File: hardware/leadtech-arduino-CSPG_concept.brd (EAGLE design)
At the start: 80 x 61 mm, 63 parts, among them IC1 OP-AMP, IC3 4050D, J1 CON_HEADER_1X08-PTH, J3 CON_HX42003_2, J5 CON_HEADER_1X02-PTH, J6 2510-4AGW, J9 CON_HEADER_1X02-PTH, Q1 16Mhz, U1 DS1302, U2 VREG-78M05, U3 PL2303HX, U4 MP1584EN_MODULE, U5 RT9163-3.3V, U6 ATMEGA1281, U7 AZ1117CH2-3.3TRG1

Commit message: 1
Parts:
- moved J3 10.7 mm to (66.2, 57.0)
- moved U2 7.24 mm to (63.5, 48.9), turned to 270 degrees
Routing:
- net +5V: track 221.0 -> 239.4 mm
- net VIN: track 44.7 -> 48.7 mm
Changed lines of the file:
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@@
 <?xml version="1.0" encoding="utf-8"?>
 <!DOCTYPE eagle SYSTEM "eagle.dtd">
-<eagle version="9.4.2">
+<eagle version="9.1.3">
 <drawing>
 <settings>
@@
 <attribute name="VALUE" x="57.912" y="21.971" size="1.27" layer="27" font="vector" ratio="10" rot="R180"/>
 </element>
-<element name="U2" library="trosh_devices.eagle.v9" package="DPAK-3" value="VREG-78M05" x="65.405" y="55.88" smashed="yes">
-<attribute name="NAME" x="65.405" y="45.72" size="1.27" layer="25" font="vector" ratio="12" rot="R180" align="center"/>
-<attribute name="VALUE" x="65.405" y="45.72" size="1.27" layer="27" font="vector" align="center"/>
+<element name="U2" library="trosh_devices.eagle.v9" package="DPAK-3" value="VREG-78M05" x="63.5" y="48.895" smashed="yes" rot="R270">
+<attribute name="NAME" x="53.34" y="48.895" size="1.27" layer="25" font="vector" ratio="12" rot="R90" align="center"/>
+<attribute name="VALUE" x="53.34" y="48.895" size="1.27" layer="27" font="vector" rot="R270" align="center"/>
 </element>
 <element name="U4" library="trosh_devices.eagle.v9" package="MP1584EN_DCDC_MODULE" value="MP1584EN_MODULE" x="67.905" y="32.385" smashed="yes" rot="R180">
@@
 <attribute name="VALUE" x="6.604" y="26.162" size="1.27" layer="27" font="vector" ratio="10" rot="R270"/>
 </element>
-<element name="J3" library="trosh_devices.eagle.v9" package="HX42003-2WAF" value="CON_HX42003_2" x="76.835" y="57.15" smashed="yes" rot="R90">
-<attribute name="NAME" x="78.105" y="60.96" size="1.27" layer="25" rot="R90"/>
-<attribute name="VALUE" x="80.645" y="60.96" size="1.27" layer="27" rot="R90"/>
+<element name="J3" library="trosh_devices.eagle.v9" package="HX42003-2WAF" value="CON_HX42003_2" x="66.167" y="57.023" smashed="yes" rot="R90">
+<attribute name="NAME" x="67.437" y="60.833" size="1.27" layer="25" rot="R90"/>
+<attribute name="VALUE" x="69.977" y="60.833" size="1.27" layer="27" rot="R90"/>
 </element>
 <element name="J6" library="trosh_devices.eagle.v9" package="KF2510-4AGW-2" value="2510-4AGW" x="11.811" y="51.435" smashed="yes" rot="R90">
@@
 <wire x1="59.385" y1="44.45" x2="63.5" y2="44.45" width="1.2192" layer="1"/>
 <wire x1="63.5" y1="44.45" x2="66.675" y2="44.45" width="1.2192" layer="1"/>
-<wire x1="67.69" y1="45.465" x2="67.69" y2="48.7" width="1.2192" layer="1"/>
+<wire x1="67.69" y1="45.465" x2="56.32" y2="46.61" width="1.2192" layer="1"/>
 <wire x1="66.675" y1="44.45" x2="67.69" y2="45.465" width="1.2192" layer="1"/>
 <wire x1="57.565" y1="59.015" x2="59.73" y2="59.015" width="0.3048" layer="1"/>
 <wire x1="60.96" y1="57.785" x2="60.96" y2="52.07" width="0.3048" layer="1"/>
 <wire x1="60.96" y1="52.07" x2="61.595" y2="51.435" width="0.3048" layer="1"/>
-<wire x1="67.69" y1="50.42" x2="67.69" y2="48.7" width="0.3048" layer="1"/>
+<wire x1="67.69" y1="50.42" x2="56.32" y2="46.61" width="0.3048" layer="1"/>
 <wire x1="59.73" y1="59.015" x2="60.96" y2="57.785" width="0.3048" layer="1"/>
 <wire x1="61.595" y1="51.435" x2="66.675" y2="51.435" width="0.3048" layer="1"/>
@@
 <contactref element="R11" pad="2"/>
 <contactref element="U2" pad="1"/>
-<wire x1="63.12" y1="48.7" x2="61.485" y2="48.7" width="1.2192" layer="1"/>
+<wire x1="56.32" y1="51.18" x2="61.485" y2="48.7" width="1.2192" layer="1"/>
 <wire x1="61.485" y1="48.7" x2="59.385" y2="50.8" width="1.2192" layer="1"/>
 <wire x1="53.34" y1="52.665" x2="58.46" y2="52.665" width="1.2192" layer="1"/>
@@
 <wire x1="78.105" y1="40.236" x2="77.176" y2="39.307" width="1.2192" layer="1"/>
 <contactref element="J3" pad="1"/>
-<wire x1="78.105" y1="52.03" x2="71.335" y2="57.15" width="0" layer="19" extent="1-1"/>
+<wire x1="78.105" y1="52.03" x2="60.667" y2="57.023" width="0" layer="19" extent="1-1"/>
 </signal>
 <signal name="N$20">

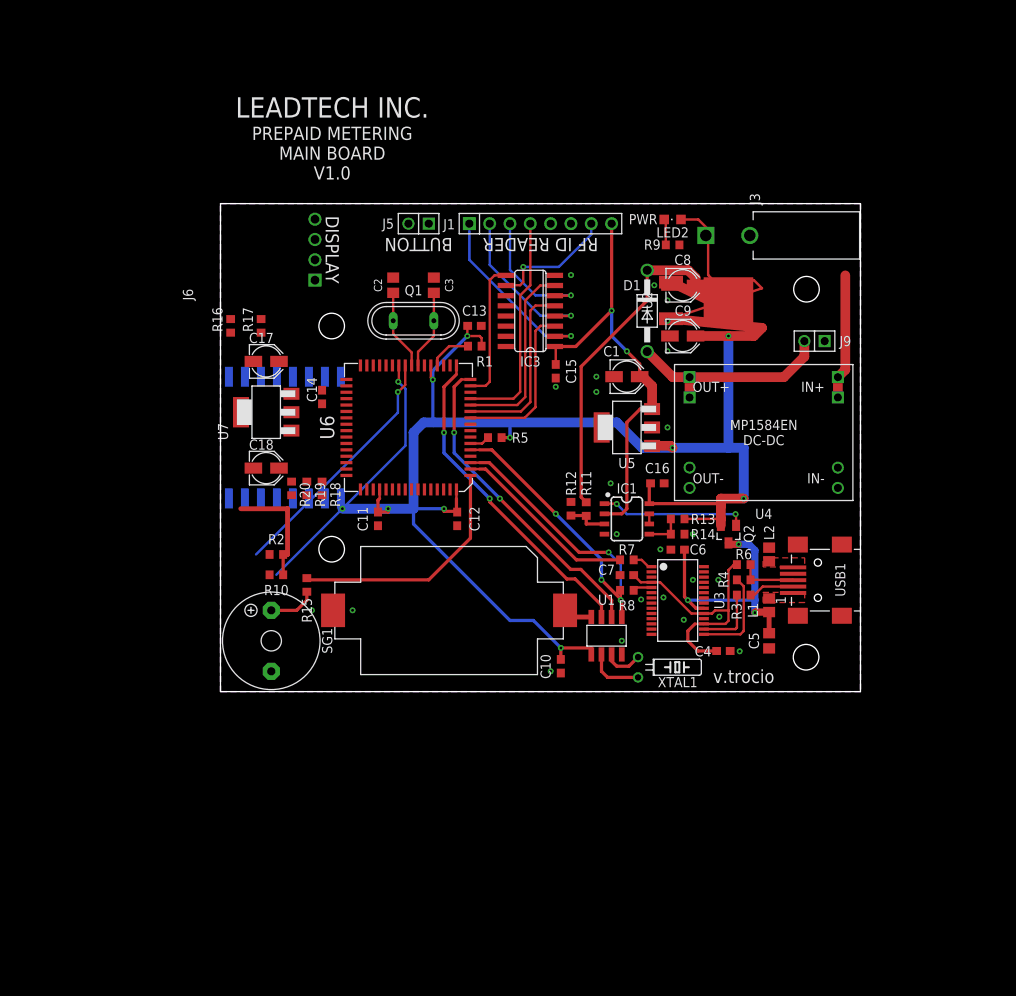
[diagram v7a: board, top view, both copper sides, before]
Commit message: done routing, add bom
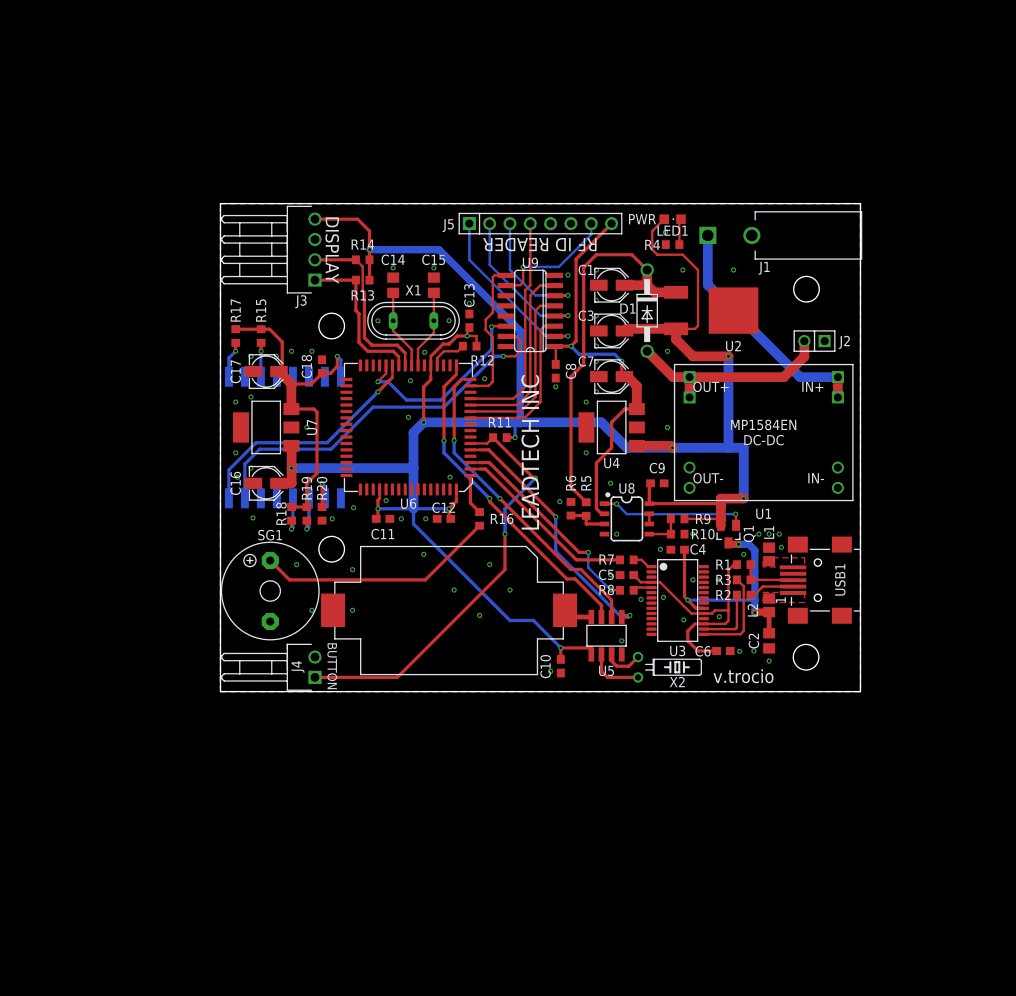
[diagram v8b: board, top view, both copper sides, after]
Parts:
- removed J6: 2510-4AGW, trosh_devices.eagle.v9:KF2510-4AGW-2
- removed LED2: (no value), dp_devices.v6:LED-805
- removed Q2: (no value), dp_devices.v6:SOT-23
- added J4: CON_KF2510-2AGW, trosh_devices.eagle.v9:KF2510-2AGW
- added LED1: (no value), dp_devices.v6:LED-805
- added X1: 16Mhz, special:QS
- C14, C15: value 0.1uF -> 22pF; device rcl:C0603 -> dp_devices.v6:C805
- C16: value 0.1uF -> 10uF; device rcl:C0603 -> dp_devices.v6:CASE_B
- C18: value 10uF -> 0.1uF; device dp_devices.v6:CASE_B -> rcl:C0603
- C2: value 22pF -> 10uF; device dp_devices.v6:C805 -> rcl:C0805
- C3: value 22pF -> 100uF; device dp_devices.v6:C805 -> dp_devices.v6:CASE_B
- C5: value 10uF -> 0.1uF; device rcl:C0805 -> rcl:C0603
- C7: value 0.1uF -> 100uF; device rcl:C0603 -> dp_devices.v6:CASE_B
- C8, C9: value 100uF -> 0.1uF; device dp_devices.v6:CASE_B -> rcl:C0603
- J1: value CON_HEADER_1X08-PTH -> CON_HX42003_2; device dp_devices.v6:M1X8 -> trosh_devices.eagle.v9:HX42003-2WAF
- J3: value CON_HX42003_2 -> 2510-4AGW; device trosh_devices.eagle.v9:HX42003-2WAF -> trosh_devices.eagle.v9:KF2510-4AGW-2
- J5: value CON_HEADER_1X02-PTH -> CON_HEADER_1X08-PTH; device dp_devices.v6:M1X2 -> dp_devices.v6:M1X8
- Q1: value 16Mhz -> (none); device special:QS -> dp_devices.v6:SOT-23
- R1: value 10K -> 1.5K; device rcl:R0603 -> dp_devices.v6:R603
- R10, R5: device rcl:R0603 -> dp_devices.v6:R603
- R11, R12, R13, R14: device dp_devices.v6:R603 -> rcl:R0603
- R15: value 100R -> 10K; device rcl:R0603 -> dp_devices.v6:R603
- R16: value 10K -> 100R; device dp_devices.v6:R603 -> rcl:R0603
- R2: value 10K -> 27R; device rcl:R0603 -> dp_devices.v6:R603
- R4: value 27R -> 330R
- R6: value 1.5K -> 10K
- R9: value 330R -> 10K
- U1: value DS1302 -> MP1584EN_MODULE; device trosh_devices.eagle.v9:SOIC-8 -> trosh_devices.eagle.v9:MP1584EN_DCDC_MODULE
- U4: value MP1584EN_MODULE -> RT9163-3.3V; device trosh_devices.eagle.v9:MP1584EN_DCDC_MODULE -> trosh_devices.eagle.v9:SOT-223
- U5: value RT9163-3.3V -> DS1302; device trosh_devices.eagle.v9:SOT-223 -> trosh_devices.eagle.v9:SOIC-8
- moved C2 64.7 mm to (68.6, 6.35), turned to 270 degrees
- moved R2 58.6 mm to (65.4, 12.1), turned to 180 degrees
- moved J3 54.6 mm to (11.8, 51.4)
- moved R14 52.2 mm to (17.8, 54.0), turned to 0 degrees
- moved R10 50.4 mm to (57.1, 19.7), turned to 180 degrees
- moved R13 49.4 mm to (17.8, 51.4)
- moved C16 48.9 mm to (5.71, 26.0), turned to 0 degrees
- moved Q1 47.6 mm to (63.5, 19.7), turned to 180 degrees
- moved R1 43.3 mm to (65.4, 15.9), turned to 180 degrees
- moved R4 42.8 mm to (56.5, 55.9)
- moved R16 39.4 mm to (32.4, 21.6), turned to 270 degrees
- moved R9 34.3 mm to (57.1, 21.6)
- moved U1 32.1 mm to (67.9, 32.4), turned to 180 degrees
- moved R15 31.6 mm to (5.08, 44.5), turned to 90 degrees
- moved J1 26.5 mm to (66.4, 57.0), turned to 90 degrees
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- renumbered IC1 to U8, IC3 to U9, J9 to J2, MOD1 to U10, XTAL1 to X2
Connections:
- net +3V3: now also C7.+, C8.2, J5.8, U4.3; no longer C1.+, C15.2, J1.8, R16.2, R17.2, R19.1, R20.1, U5.3
- net +3V3_ESP: now also C18.2, R15.2, R17.2, R18.1, R19.1; no longer C14.2
- net +5V: now also C16.+, C3.+, C9.2, J3.4, LED1.A, Q1.2, R11.2, R12.2, R14.2, R9.2, U4.1, U5.P1; no longer C16.2, C18.+, C9.+, J6.4, LED2.A, Q2.2, R1.2, R10.2, R2.2, R5.2, U1.P1, U5.1
- net DISPLAY_I2C_CLOCK: now also J3.2, R14.1; no longer J6.2, R2.1
- net DISPLAY_I2C_DATA: now also J3.1, R13.1; no longer J6.1, R10.1
- net GND: now also C14.2, C16.-, C18.1, C3.-, C4.1, C6.2, C7.-, C8.1, C9.1, J1.2, J3.3, J4.2, J5.6, L1.1, R10.1, R20.1, R4.2, R6.1, U1.1, U1.2, U1.7, U1.8, U4.4, U5.P4; no longer C14.1, C16.1, C18.-, C3.1, C4.2, C6.1, C7.2, C8.-, C9.-, J1.6, J3.2, J5.2, J6.3, L2.1, R12.1, R14.1, R18.1, R9.2, U1.P4, U4.1, U4.7, U4.8, U5.2, U5.4
- net N$1: now also R17.1; no longer R16.1
- net N$10: now also C14.1, X1.1; no longer C2.1, Q1.1
- net N$11: now also R2.1; no longer R3.1
- net N$12: now also R1.1, R3.1; no longer R4.1, R6.1
- net N$13: now also R2.2; no longer R3.2
- net N$14: now also R3.2; no longer R4.2
- net N$15: now also L2.2; no longer L1.2
- net N$16: now also L1.2; no longer L2.2
- net N$19: now also U1.5, U1.6; no longer U4.5, U4.6
- net N$2: now also R15.1; no longer R17.1
- net N$20: now also R16.2; no longer R15.2
- net N$21: now also LED1.C, R4.1; no longer LED2.C, R9.1
- net N$22: now also U5.P3; no longer U1.P3
- net N$23: now also U5.P2; no longer U1.P2
- net N$24: now also U5.P8; no longer U1.P8
- net N$25: now also R20.2; no longer R18.2
- net N$27: now also R18.2; no longer R20.2
- net N$3: now also R12.1; no longer R1.1
- net N$4: now also Q1.1; no longer Q2.1
- net N$5: now also R5.1, R6.2; no longer R11.1, R12.2
- net N$7: now also J1.1, U1.3, U1.4; no longer J3.1, U4.3, U4.4
- net N$8: now also C15.2, X1.2; no longer C3.2, Q1.2
- net N$9: now also R10.2, R9.1; no longer R13.1, R14.2
- net PIEZO: now also R16.1; no longer R15.1
- net RFID_CLOCK_3V: now also J5.2; no longer J1.2
- net RFID_DATA_3V: now also J5.1; no longer J1.1
- net RFID_MISO: now also J5.4; no longer J1.4
- net RFID_MOSI_3V: now also J5.3; no longer J1.3
- net RFID_RESET_3V: now also J5.7; no longer J1.7
- net RTC_CLOCK: now also U5.P7; no longer U1.P7
- net RTC_DATA: now also U5.P6; no longer U1.P6
- net RTC_EN: now also U5.P5; no longer U1.P5
- net SW1: now also J4.1, R11.1; no longer J5.1, R5.1
- net VIN: now also C1.+, R5.2; no longer C8.+, R11.2
- net VO33: now also C5.1, C6.1, R1.2; no longer C4.1, C7.1, R6.2
- net VUSB: now also C2.1, C4.2, L2.1, Q1.3; no longer C5.1, C6.2, L1.1, Q2.3
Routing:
- net SW1: track 2.50 -> 52.9 mm, vias 0 -> 2
- net N$28: track 0.00 -> 47.9 mm, vias 0 -> 1
- net +3V3_ESP: track 0.00 -> 44.0 mm, vias 0 -> 1
- net +5V: track 239.4 -> 274.5 mm, vias 10 -> 11
- net ESP_TXD: track 0.00 -> 30.3 mm, vias 0 -> 1
- net PIEZO: track 30.5 -> 5.05 mm
- net ESP_RXD: track 0.00 -> 24.8 mm, vias 0 -> 2
- net N$20: track 6.03 -> 30.0 mm
- net N$7: track 15.6 -> 29.8 mm
- net DISPLAY_I2C_DATA: track 33.2 -> 19.9 mm, vias 1 -> 0
- net DISPLAY_I2C_CLOCK: track 31.4 -> 22.7 mm, vias 1 -> 0
- net N$26: track 0.00 -> 4.99 mm, vias 0 -> 1
- net N$25: track 0.00 -> 4.99 mm, vias 0 -> 1
- net N$27: track 0.00 -> 4.95 mm, vias 0 -> 1
- net N$1: track 0.00 -> 4.60 mm, vias 0 -> 1
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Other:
- board text added: "LEADTECH INC"
- board text removed: "LEADTECH INC."
